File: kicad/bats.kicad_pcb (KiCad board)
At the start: 2 copper layers, 68.9 x 53.6 mm, 24 parts, among them P1 SERVO, SW1 RESET, SW2 SHOT, SW4 LEFT, SW6 RIGHT, U1 BUZZER

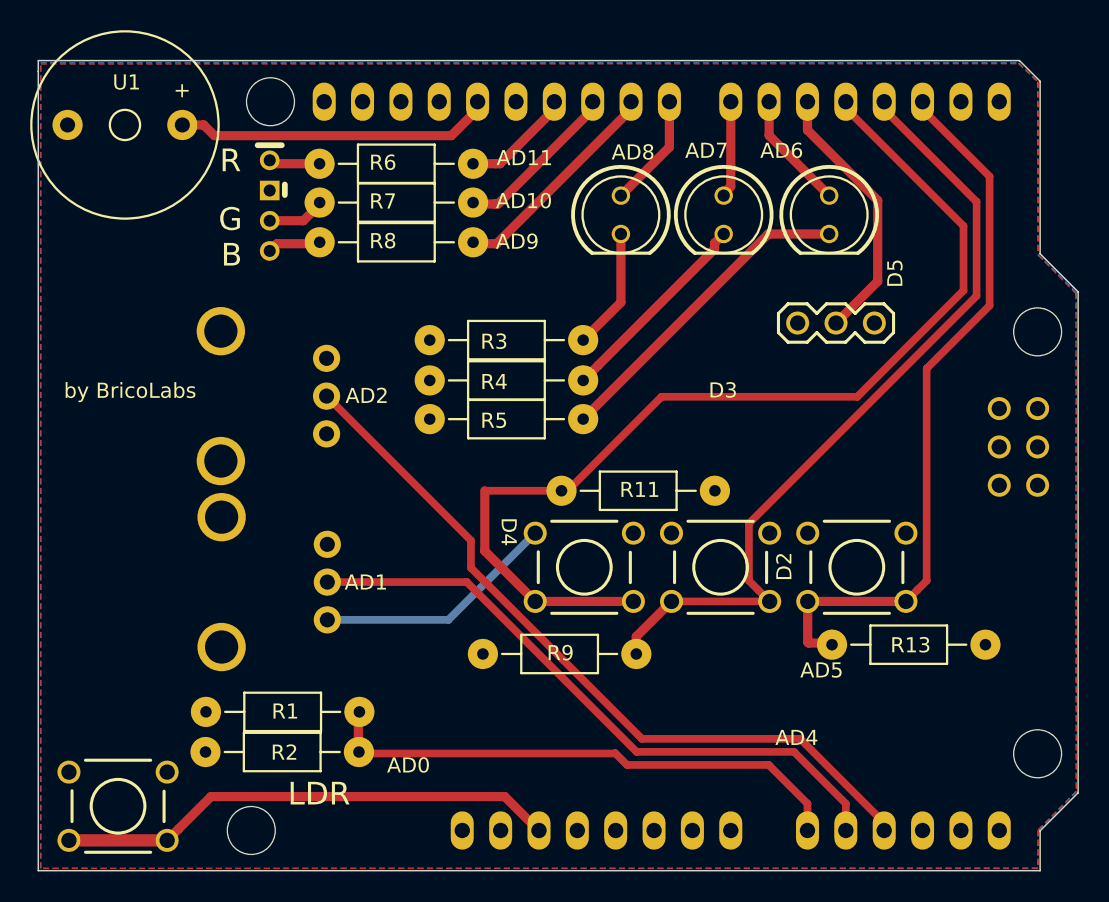
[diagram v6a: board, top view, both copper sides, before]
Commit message: TEN UN FALLO, non usar sen cambiar o botón en D1
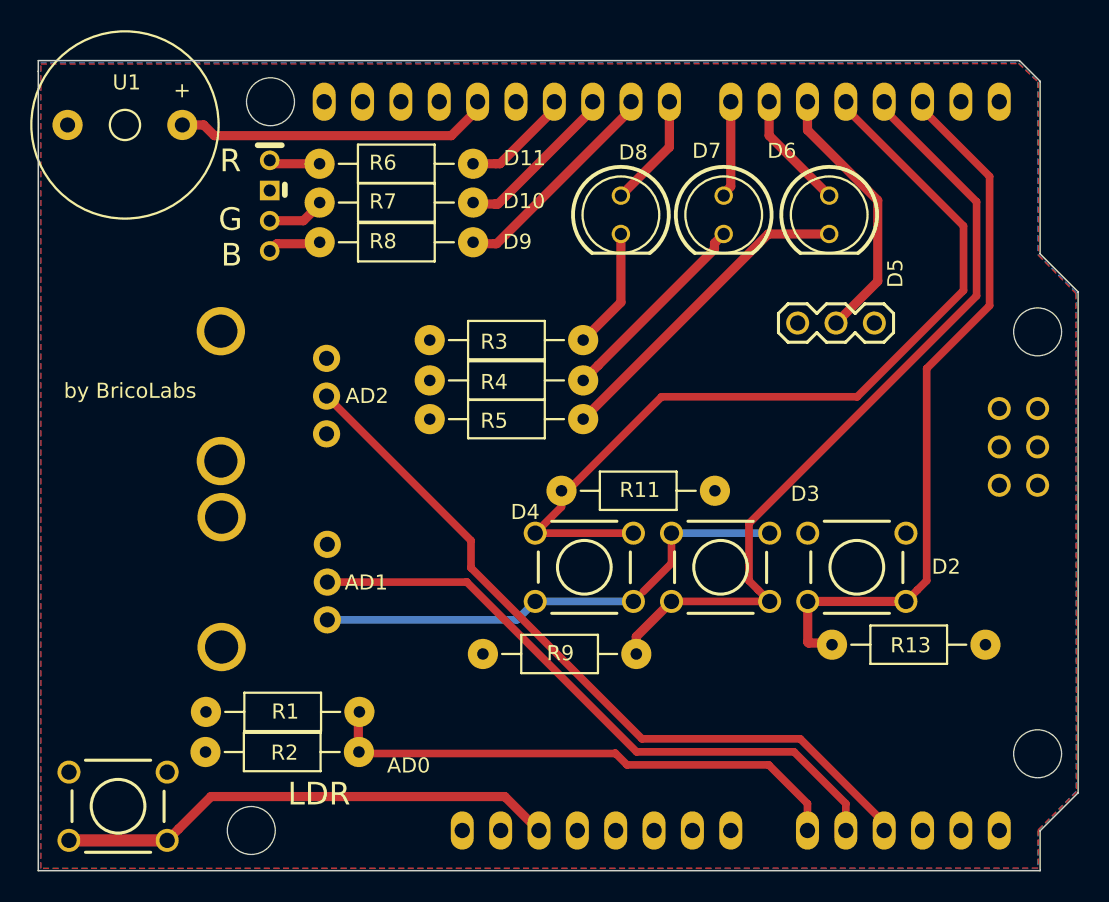
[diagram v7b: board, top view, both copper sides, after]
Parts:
- turned SW4 to 180 degrees
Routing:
- net /VCC: track 16.1 -> 31.9 mm
- net /ARD4: track 68.1 -> 57.5 mm
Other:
- board text added: "D10"
- board text added: "D11"
- board text added: "D6"
- board text added: "D7"
- board text added: "D8"
- board text added: "D9"
- board text removed: "AD10"
- board text removed: "AD11"
- board text removed: "AD4"
- board text removed: "AD5"
- board text removed: "AD6"
- board text removed: "AD7"
- board text removed: "AD8"
- board text removed: "AD9"
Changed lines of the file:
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@@
   (general
     (links 55)
-    (no_connects 1)
+    (no_connects 0)
     (area 126.772199 84.227199 195.731601 137.972001)
     (thickness 1.6)
-    (drawings 30)
-    (tracks 107)
+    (drawings 28)
+    (tracks 110)
     (zones 0)
     (modules 24)
@@
   )
   (module FT:SW_PUSHBUTTON_PTH (layer F.Cu)
-    (at 162.98164 117.8306)
+    (at 162.98164 117.8306 180)
     (descr "<b>OMRON SWITCH</b>")
-    (fp_text reference SW4 (at -0.05 0) (layer Eco1.User)
-      (effects (font (size 0.6 0.6) (thickness 0.1)))
-    )
-    (fp_text value LEFT (at 0 0) (layer Eco1.User) hide
+    (fp_text reference SW4 (at -0.05 0 180) (layer Eco1.User)
+      (effects (font (size 0.6 0.6) (thickness 0.1)))
+    )
+    (fp_text value LEFT (at 0 0 180) (layer Eco1.User) hide
       (effects (font (size 0 0) (thickness 0.000001)))
     )
@@
     (fp_line (start -2.54 -0.508) (end -2.159 0.381) (layer Cmts.User) (width 0.2032))
     (fp_circle (center 0 0) (end 1.778 0) (layer F.SilkS) (width 0.2032))
-    (pad 1 thru_hole oval (at -3.2512 -2.2606) (size 1.524 1.524) (drill 1.016) (layers *.Cu *.Mask)
+    (pad 1 thru_hole oval (at -3.2512 -2.2606 180) (size 1.524 1.524) (drill 1.016) (layers *.Cu *.Mask)
       (net 35 /VCC))
-    (pad 1 thru_hole oval (at 3.2512 -2.2606) (size 1.524 1.524) (drill 1.016) (layers *.Cu *.Mask)
+    (pad 1 thru_hole oval (at 3.2512 -2.2606 180) (size 1.524 1.524) (drill 1.016) (layers *.Cu *.Mask)
       (net 35 /VCC))
-    (pad 2 thru_hole oval (at -3.2512 2.2606) (size 1.524 1.524) (drill 1.016) (layers *.Cu *.Mask)
+    (pad 2 thru_hole oval (at -3.2512 2.2606 180) (size 1.524 1.524) (drill 1.016) (layers *.Cu *.Mask)
       (net 19 /ARD4))
-    (pad 2 thru_hole oval (at 3.2512 2.2606) (size 1.524 1.524) (drill 1.016) (layers *.Cu *.Mask)
+    (pad 2 thru_hole oval (at 3.2512 2.2606 180) (size 1.524 1.524) (drill 1.016) (layers *.Cu *.Mask)
       (net 19 /ARD4))
   )
@@
       (net 3 "Net-(LED3-PadK)"))
   )
-  (gr_text AD6 (at 176.0601 90.25382) (layer F.SilkS)
+  (gr_text D6 (at 176.0601 90.25382) (layer F.SilkS)
     (effects (font (size 1 1) (thickness 0.25)))
   )
-  (gr_text AD7 (at 171.08678 90.25382) (layer F.SilkS)
+  (gr_text D7 (at 171.08678 90.25382) (layer F.SilkS)
     (effects (font (size 1 1) (thickness 0.25)))
   )
-  (gr_text AD8 (at 166.22014 90.3605) (layer F.SilkS)
+  (gr_text D8 (at 166.22014 90.3605) (layer F.SilkS)
     (effects (font (size 1 1) (thickness 0.25)))
   )
-  (gr_text AD9 (at 158.55188 96.27616) (layer F.SilkS)
+  (gr_text D9 (at 158.55188 96.27616) (layer F.SilkS)
     (effects (font (size 1 1) (thickness 0.25)))
   )
-  (gr_text AD10 (at 158.99384 93.58376) (layer F.SilkS)
+  (gr_text D10 (at 158.99384 93.58376) (layer F.SilkS)
     (effects (font (size 1 1) (thickness 0.25)))
   )
-  (gr_text AD11 (at 159.03448 90.73896) (layer F.SilkS)
+  (gr_text D11 (at 159.03448 90.73896) (layer F.SilkS)
     (effects (font (size 1 1) (thickness 0.25)))
   )
@@
     (effects (font (size 1.5 1.5) (thickness 0.3)))
   )
-  (gr_text D2 (at 176.23028 117.7798 90) (layer F.SilkS)
+  (gr_text D3 (at 177.6095 112.9665) (layer F.SilkS)
     (effects (font (size 1 1) (thickness 0.15)))
   )
-  (gr_text D3 (at 172.16628 106.1212) (layer F.SilkS)
-    (effects (font (size 1 1) (thickness 0.15)))
-  )
-  (gr_text D4 (at 157.97276 115.48364 270) (layer F.SilkS)
+  (gr_text D4 (at 159.0675 114.173) (layer F.SilkS)
     (effects (font (size 1 1) (thickness 0.15)))
   )
@@
     (effects (font (size 1 1) (thickness 0.15)))
   )
-  (gr_text AD5 (at 178.70932 124.6632) (layer F.SilkS)
-    (effects (font (size 1 1) (thickness 0.15)))
-  )
-  (gr_text AD4 (at 177.05832 129.1336) (layer F.SilkS)
+  (gr_text D2 (at 186.944 117.7925) (layer F.SilkS)
     (effects (font (size 1 1) (thickness 0.15)))
   )
@@
   (segment (start 168.75379 120.0912) (end 166.42334 122.42165) (width 0.6096) (layer F.Cu) (net 18))
   (segment (start 166.42334 122.42165) (end 166.42334 123.5837) (width 0.6096) (layer F.Cu) (net 18))
-  (segment (start 161.87242 112.7633) (end 156.39034 112.7633) (width 0.508) (layer F.Cu) (net 19))
+  (segment (start 161.47034 112.7633) (end 161.47034 113.8301) (width 0.508) (layer F.Cu) (net 19))
+  (segment (start 161.47034 113.8301) (end 159.73044 115.57) (width 0.508) (layer F.Cu) (net 19))
+  (segment (start 166.23284 115.57) (end 159.73044 115.57) (width 0.508) (layer F.Cu) (net 19))
   (segment (start 168.095421 106.540299) (end 161.87242 112.7633) (width 0.508) (layer F.Cu) (net 19))
-  (segment (start 166.23284 120.0912) (end 159.73044 120.0912) (width 0.6096) (layer F.Cu) (net 19))
-  (segment (start 159.73044 120.0912) (end 156.39034 116.7511) (width 0.6096) (layer F.Cu) (net 19))
-  (segment (start 156.39034 116.7511) (end 156.39034 112.7633) (width 0.6096) (layer F.Cu) (net 19))
   (segment (start 180.29936 87.00008) (end 180.29936 87.436237) (width 0.508) (layer F.Cu) (net 19))
   (segment (start 180.29936 87.436237) (end 188.092441 95.229318) (width 0.508) (layer F.Cu) (net 19))
@@
   (segment (start 188.092441 99.501599) (end 181.053741 106.540299) (width 0.508) (layer F.Cu) (net 19))
   (segment (start 181.053741 106.540299) (end 168.095421 106.540299) (width 0.508) (layer F.Cu) (net 19))
-  (segment (start 159.73044 115.57) (end 153.9894 121.31104) (width 0.508) (layer B.Cu) (net 35))
-  (segment (start 153.9894 121.31104) (end 145.9634 121.31104) (width 0.508) (layer B.Cu) (net 35))
+  (segment (start 159.73044 120.0912) (end 166.23284 120.0912) (width 0.508) (layer B.Cu) (net 35))
+  (segment (start 145.9634 121.31104) (end 158.5106 121.31104) (width 0.508) (layer B.Cu) (net 35))
+  (segment (start 158.5106 121.31104) (end 159.73044 120.0912) (width 0.508) (layer B.Cu) (net 35))
+  (segment (start 168.75379 115.57) (end 175.25619 115.57) (width 0.508) (layer B.Cu) (net 35))
+  (segment (start 168.75379 115.57) (end 168.75379 117.570249) (width 0.508) (layer F.Cu) (net 35))
+  (segment (start 168.75379 117.570249) (end 166.879425 119.444614) (width 0.508) (layer F.Cu) (net 35))
   (segment (start 165.03396 130.13944) (end 165.0111 130.1623) (width 0.508) (layer F.Cu) (net 36))
   (segment (start 165.0111 130.1623) (end 148.0312 130.1623) (width 0.508) (layer F.Cu) (net 36))

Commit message: Primeira versión completa con tres botóns. Os ficheiros gerber non son válidos. - Hai que revisar a conexión do servo - Hai que alinear ben os tres botóns
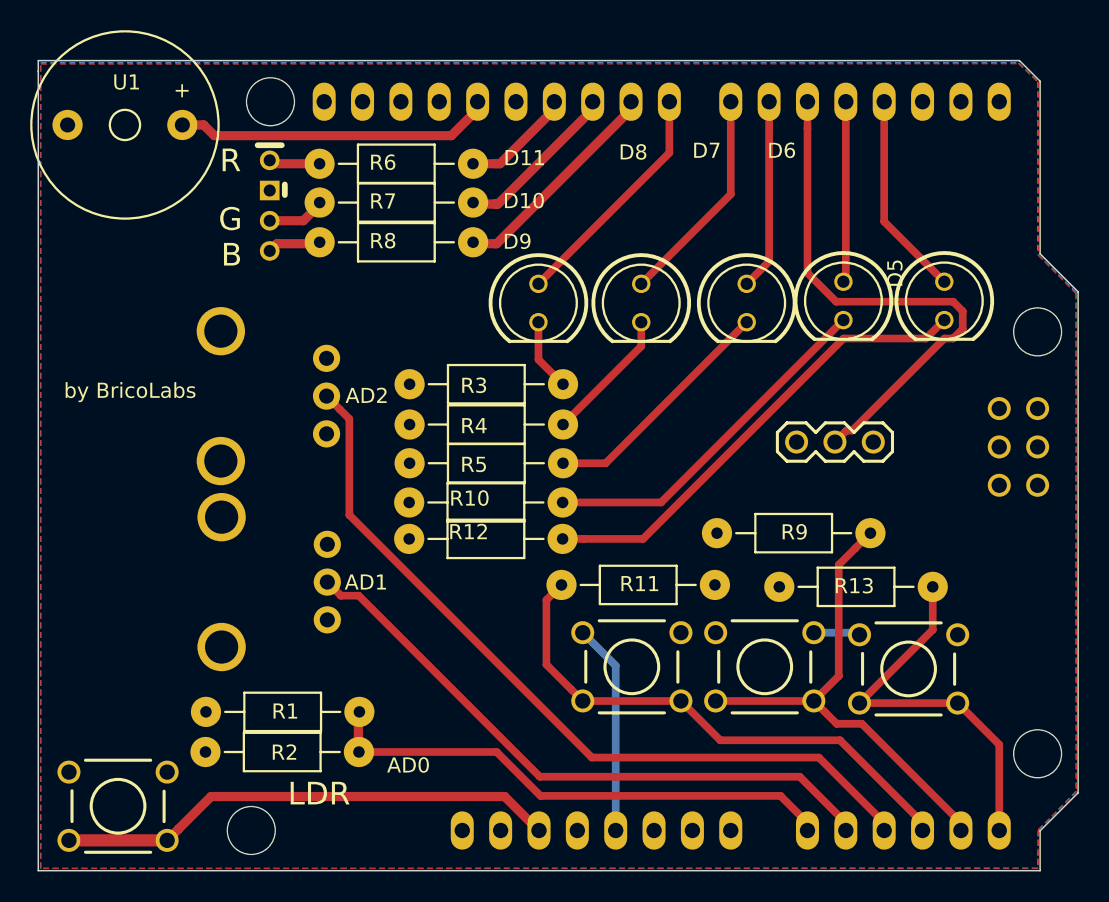
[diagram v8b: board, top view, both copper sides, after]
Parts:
- added LED5: LED, FT:LED-5MM, F.Cu at (180.1, 100.2)
- added LED6: LED, FT:LED-5MM, F.Cu at (186.8, 100.2)
- added R10: 220, extra:Resistor_Horizontal_SmallHole_RM10mm, F.Cu at (161.5, 113.5)
- added R12: 220, extra:Resistor_Horizontal_SmallHole_RM10mm, F.Cu at (161.5, 116.0)
- moved R9 17.4 mm to (181.9, 115.6)
- moved P1 9.34 mm to (182.1, 109.5), turned to 180 degrees
- moved LED3 8.00 mm to (173.7, 100.3)
- moved LED1 8.00 mm to (159.9, 100.3)
- moved LED2 8.00 mm to (166.8, 100.3)
- moved R13 7.69 mm to (186.1, 119.1), turned to 180 degrees
- moved SW6 7.55 mm to (184.5, 124.6)
- moved SW4 7.30 mm to (166.1, 124.4), turned to 0 degrees
- moved SW2 7.21 mm to (174.9, 124.4)
- moved R11 6.24 mm to (161.5, 119.0)
- moved R5 3.21 mm to (161.6, 110.9)
- moved R3 3.21 mm to (161.6, 105.7)
- moved R4 3.21 mm to (161.6, 108.4)
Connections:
- R11 pad 1: /ARD4 -> /AD3
- R13 pad 1: /ARD2 -> /AD5
- R9 pad 1: /ARD3 -> /AD4
- SHIELD1 pad 0: Net-(SHIELD1-Pad0) -> (no net)
- SHIELD1 pad 1: Net-(SHIELD1-Pad1) -> (no net)
- SHIELD1 pad 12: Net-(SHIELD1-Pad12) -> (no net)
- SHIELD1 pad 2: /ARD2 -> (no net)
- SHIELD1 pad 3V3: Net-(SHIELD1-Pad3V3) -> (no net)
- SHIELD1 pad AD3: Net-(SHIELD1-PadAD3) -> /AD3
- SHIELD1 pad AD4: Net-(SHIELD1-PadAD4) -> /AD4
- SHIELD1 pad AD5: Net-(SHIELD1-PadAD5) -> /AD5
- SHIELD1 pad AREF: Net-(SHIELD1-PadAREF) -> (no net)
- SHIELD1 pad IO_R: Net-(SHIELD1-PadIO_R) -> (no net)
- SHIELD1 pad NC: Net-(SHIELD1-PadNC) -> (no net)
- SHIELD1 pad SCL: Net-(SHIELD1-PadSCL) -> (no net)
- SHIELD1 pad SDA: Net-(SHIELD1-PadSDA) -> (no net)
- SHIELD1 pad SP1: Net-(SHIELD1-PadSP1) -> (no net)
- SHIELD1 pad SP2: Net-(SHIELD1-PadSP2) -> (no net)
- SHIELD1 pad SP3: Net-(SHIELD1-PadSP3) -> (no net)
- SHIELD1 pad SP4: Net-(SHIELD1-PadSP4) -> (no net)
- SHIELD1 pad SP5: Net-(SHIELD1-PadSP5) -> (no net)
- SHIELD1 pad SP6: Net-(SHIELD1-PadSP6) -> (no net)
- SHIELD1 pad V_IN: Net-(SHIELD1-PadV_IN) -> (no net)
- SW2 pad 2: /ARD3 -> /AD4
- SW4 pad 2: /ARD4 -> /AD3
- SW6 pad 2: /ARD2 -> /AD5
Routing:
- net /ARD2: track 47.9 -> 0.00 mm
- net /ARD4: track 57.5 -> 12.0 mm
- net /ARD3: track 53.4 -> 13.6 mm
- net /AD3: track 0.00 -> 35.4 mm
- net /AD4: track 0.00 -> 32.8 mm
- net Net-(LED6-PadK): track 0.00 -> 31.3 mm
- net /AD5: track 0.00 -> 25.8 mm
- net Net-(LED5-PadK): track 0.00 -> 23.6 mm
- net /ARD5: track 17.7 -> 35.4 mm
- net /VCC: track 31.9 -> 17.1 mm
- net /ARD7: track 6.27 -> 14.5 mm
- net /ARD8: track 7.55 -> 15.7 mm
- net Net-(LED3-PadK): track 21.4 -> 16.0 mm
- net /ARD6: track 7.87 -> 12.7 mm
- net Net-(LED2-PadK): track 13.6 -> 8.92 mm
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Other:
- board text removed: "D2"
- board text removed: "D3"
- board text removed: "D4"
